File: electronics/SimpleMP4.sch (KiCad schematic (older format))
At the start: 124 parts, among them J1 USB_OTG, J2 DISPLAY, Q1 8050, Q2 SI2305, Q3 SI2305, Q4 8050, Q5 8550, Q6 SI2305, Q7 8550, U1 OCP8020, U2 RK2608, U3 OCP2150TW18A, U4 OCP1240, U5 MT25QL128ABA, U6 K9HCG08U1M-PCB0/PIB0, U7 K4S641632N, U8 TRS_5PIN, U9 MMC/SD_SOCKET, Y1 24MHz

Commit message: added partial routing
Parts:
- L3, L5: footprint (none) -> Inductors_SMD:L_1210
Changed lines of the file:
@@
 F 0 "L5" V 8400 8000 50  0000 C CNN
 F 1 "10uH" V 8525 8000 50  0000 C CNN
-F 2 "" H 8450 8000 50  0001 C CNN
+F 2 "Inductors_SMD:L_1210" H 8450 8000 50  0001 C CNN
 F 3 "" H 8450 8000 50  0001 C CNN
 	1    8450 8000
@@
 F 0 "L3" V 7650 7500 50  0000 C CNN
 F 1 "10uH" V 7775 7500 50  0000 C CNN
-F 2 "" H 7700 7500 50  0001 C CNN
+F 2 "Inductors_SMD:L_1210" H 7700 7500 50  0001 C CNN
 F 3 "" H 7700 7500 50  0001 C CNN
 	1    7700 7500

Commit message: added test points
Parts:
- removed RN1: 5R, Resistors_THT:R_Array_SIP5, symbol R_Network04
- removed RN2: 33R*4, symbol R_Pack04
- added R37, R38, R39, R40: 33R, Resistors_SMD:R_0603, symbol R
- added R41, R42, R43, R44: R*, Resistors_SMD:R_0603, symbol R
- added TP? (x9): TEST, symbol TEST
- B1, B2, B3, B4, B5, B6: footprint SKHLAAA010:SKHLAAA010 -> HP0315AFKP4-R:SW_HP0315AFKP4-R
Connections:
- net BATT: now also TP?.1
- net FALE/RS/A1: now also R38.2
- net GND: now also TP?.1
- net I2C_SCL: now also TP?.1
- net I2C_SDA: now also TP?.1
- net LCDCSN: now also R37.2
- net LCDRDN: now also R40.2
- net LCDWRN: now also R39.2
- net PWR_ON: now also TP?.1
- net SDCLK: now also TP?.1
- net SDDI: now also TP?.1
- net SDDO: now also TP?.1
- net VCC: now also TP?.1
- net at J2.10 (P10): now also R40.1
- net at J2.17 (P17): now also R41.1
- net at J2.18 (P18): now also R42.1
- net at J2.19 (P19): now also R43.1
- net at J2.20 (P20): now also R44.1
- net at J2.7 (P7): now also R37.1
- net at J2.8 (P8): now also R38.1
- net at J2.9 (P9): now also R39.1
- net at C43.2: now also R41.2, R42.2, R43.2, R44.2
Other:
- moved on the sheet: C43, C44, C46, C47, J2, Q7, R35, R36

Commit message: added another data bus
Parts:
- TP1: renamed from TP?; value TEST -> VCC; footprint (none) -> Connectors:PINTST
- TP2: renamed from TP?; value TEST -> GND; footprint (none) -> Connectors:PINTST
- TP3: renamed from TP?; value TEST -> SDDI; footprint (none) -> Connectors:PINTST
- TP4: renamed from TP?; value TEST -> SDDO; footprint (none) -> Connectors:PINTST
- TP5: renamed from TP?; value TEST -> SDCLK; footprint (none) -> Connectors:PINTST
- TP6: renamed from TP?; value TEST -> SDA; footprint (none) -> Connectors:PINTST
- TP7: renamed from TP?; value TEST -> SCL; footprint (none) -> Connectors:PINTST
- TP8: renamed from TP?; value TEST -> BATT; footprint (none) -> Connectors:PINTST
- TP9: renamed from TP?; value TEST -> PWR_ON; footprint (none) -> Connectors:PINTST
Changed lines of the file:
@@
 Connection ~ 13700 3050
 $Comp
-L TEST TP?
+L TEST TP1
 U 1 1 5A44E92B
 P 15450 1200
-F 0 "TP?" H 15450 1500 50  0000 C BNN
-F 1 "TEST" H 15450 1450 50  0000 C CNN
-F 2 "" H 15450 1200 50  0001 C CNN
+F 0 "TP1" H 15450 1500 50  0000 C BNN
+F 1 "VCC" H 15450 1450 50  0000 C CNN
+F 2 "Connectors:PINTST" H 15450 1200 50  0001 C CNN
 F 3 "" H 15450 1200 50  0001 C CNN
 	1    15450 1200
@@
 VCC
 $Comp
-L TEST TP?
+L TEST TP2
 U 1 1 5A44FF22
 P 15450 1400
-F 0 "TP?" H 15450 1700 50  0000 C BNN
-F 1 "TEST" H 15450 1650 50  0000 C CNN
-F 2 "" H 15450 1400 50  0001 C CNN
+F 0 "TP2" H 15450 1700 50  0000 C BNN
+F 1 "GND" H 15450 1650 50  0000 C CNN
+F 2 "Connectors:PINTST" H 15450 1400 50  0001 C CNN
 F 3 "" H 15450 1400 50  0001 C CNN
 	1    15450 1400
@@
 GND
 $Comp
-L TEST TP?
+L TEST TP3
 U 1 1 5A450D61
 P 15450 1600
-F 0 "TP?" H 15450 1900 50  0000 C BNN
-F 1 "TEST" H 15450 1850 50  0000 C CNN
-F 2 "" H 15450 1600 50  0001 C CNN
+F 0 "TP3" H 15450 1900 50  0000 C BNN
+F 1 "SDDI" H 15450 1850 50  0000 C CNN
+F 2 "Connectors:PINTST" H 15450 1600 50  0001 C CNN
 F 3 "" H 15450 1600 50  0001 C CNN
 	1    15450 1600
@@
 	15250 1600 15450 1600
 $Comp
-L TEST TP?
+L TEST TP4
 U 1 1 5A452A41
 P 15450 1800
-F 0 "TP?" H 15450 2100 50  0000 C BNN
-F 1 "TEST" H 15450 2050 50  0000 C CNN
-F 2 "" H 15450 1800 50  0001 C CNN
+F 0 "TP4" H 15450 2100 50  0000 C BNN
+F 1 "SDDO" H 15450 2050 50  0000 C CNN
+F 2 "Connectors:PINTST" H 15450 1800 50  0001 C CNN
 F 3 "" H 15450 1800 50  0001 C CNN
 	1    15450 1800
@@
 	15450 1800 15250 1800
 $Comp
-L TEST TP?
+L TEST TP5
 U 1 1 5A4542A1
 P 15450 2000
-F 0 "TP?" H 15450 2300 50  0000 C BNN
-F 1 "TEST" H 15450 2250 50  0000 C CNN
-F 2 "" H 15450 2000 50  0001 C CNN
+F 0 "TP5" H 15450 2300 50  0000 C BNN
+F 1 "SDCLK" H 15450 2250 50  0000 C CNN
+F 2 "Connectors:PINTST" H 15450 2000 50  0001 C CNN
 F 3 "" H 15450 2000 50  0001 C CNN
 	1    15450 2000
@@
 SDCLK
 $Comp
-L TEST TP?
+L TEST TP6
 U 1 1 5A455DCF
 P 15450 2200
-F 0 "TP?" H 15450 2500 50  0000 C BNN
-F 1 "TEST" H 15450 2450 50  0000 C CNN
-F 2 "" H 15450 2200 50  0001 C CNN
+F 0 "TP6" H 15450 2500 50  0000 C BNN
+F 1 "SDA" H 15450 2450 50  0000 C CNN
+F 2 "Connectors:PINTST" H 15450 2200 50  0001 C CNN
 F 3 "" H 15450 2200 50  0001 C CNN
 	1    15450 2200
@@
 	15450 2200 15200 2200
 $Comp
-L TEST TP?
+L TEST TP7
 U 1 1 5A4572CC
 P 15450 2400
-F 0 "TP?" H 15450 2700 50  0000 C BNN
-F 1 "TEST" H 15450 2650 50  0000 C CNN
-F 2 "" H 15450 2400 50  0001 C CNN
+F 0 "TP7" H 15450 2700 50  0000 C BNN
+F 1 "SCL" H 15450 2650 50  0000 C CNN
+F 2 "Connectors:PINTST" H 15450 2400 50  0001 C CNN
 F 3 "" H 15450 2400 50  0001 C CNN
 	1    15450 2400
@@
 I2C_SCL
 $Comp
-L TEST TP?
+L TEST TP8
 U 1 1 5A458D47
 P 15450 2600
-F 0 "TP?" H 15450 2900 50  0000 C BNN
-F 1 "TEST" H 15450 2850 50  0000 C CNN
-F 2 "" H 15450 2600 50  0001 C CNN
+F 0 "TP8" H 15450 2900 50  0000 C BNN
+F 1 "BATT" H 15450 2850 50  0000 C CNN
+F 2 "Connectors:PINTST" H 15450 2600 50  0001 C CNN
 F 3 "" H 15450 2600 50  0001 C CNN
 	1    15450 2600
@@
 PWR_ON
 $Comp
-L TEST TP?
+L TEST TP9
 U 1 1 5A45AAA3
 P 15450 2800
-F 0 "TP?" H 15450 3100 50  0000 C BNN
-F 1 "TEST" H 15450 3050 50  0000 C CNN
-F 2 "" H 15450 2800 50  0001 C CNN
+F 0 "TP9" H 15450 3100 50  0000 C BNN
+F 1 "PWR_ON" H 15450 3050 50  0000 C CNN
+F 2 "Connectors:PINTST" H 15450 2800 50  0001 C CNN
 F 3 "" H 15450 2800 50  0001 C CNN
 	1    15450 2800

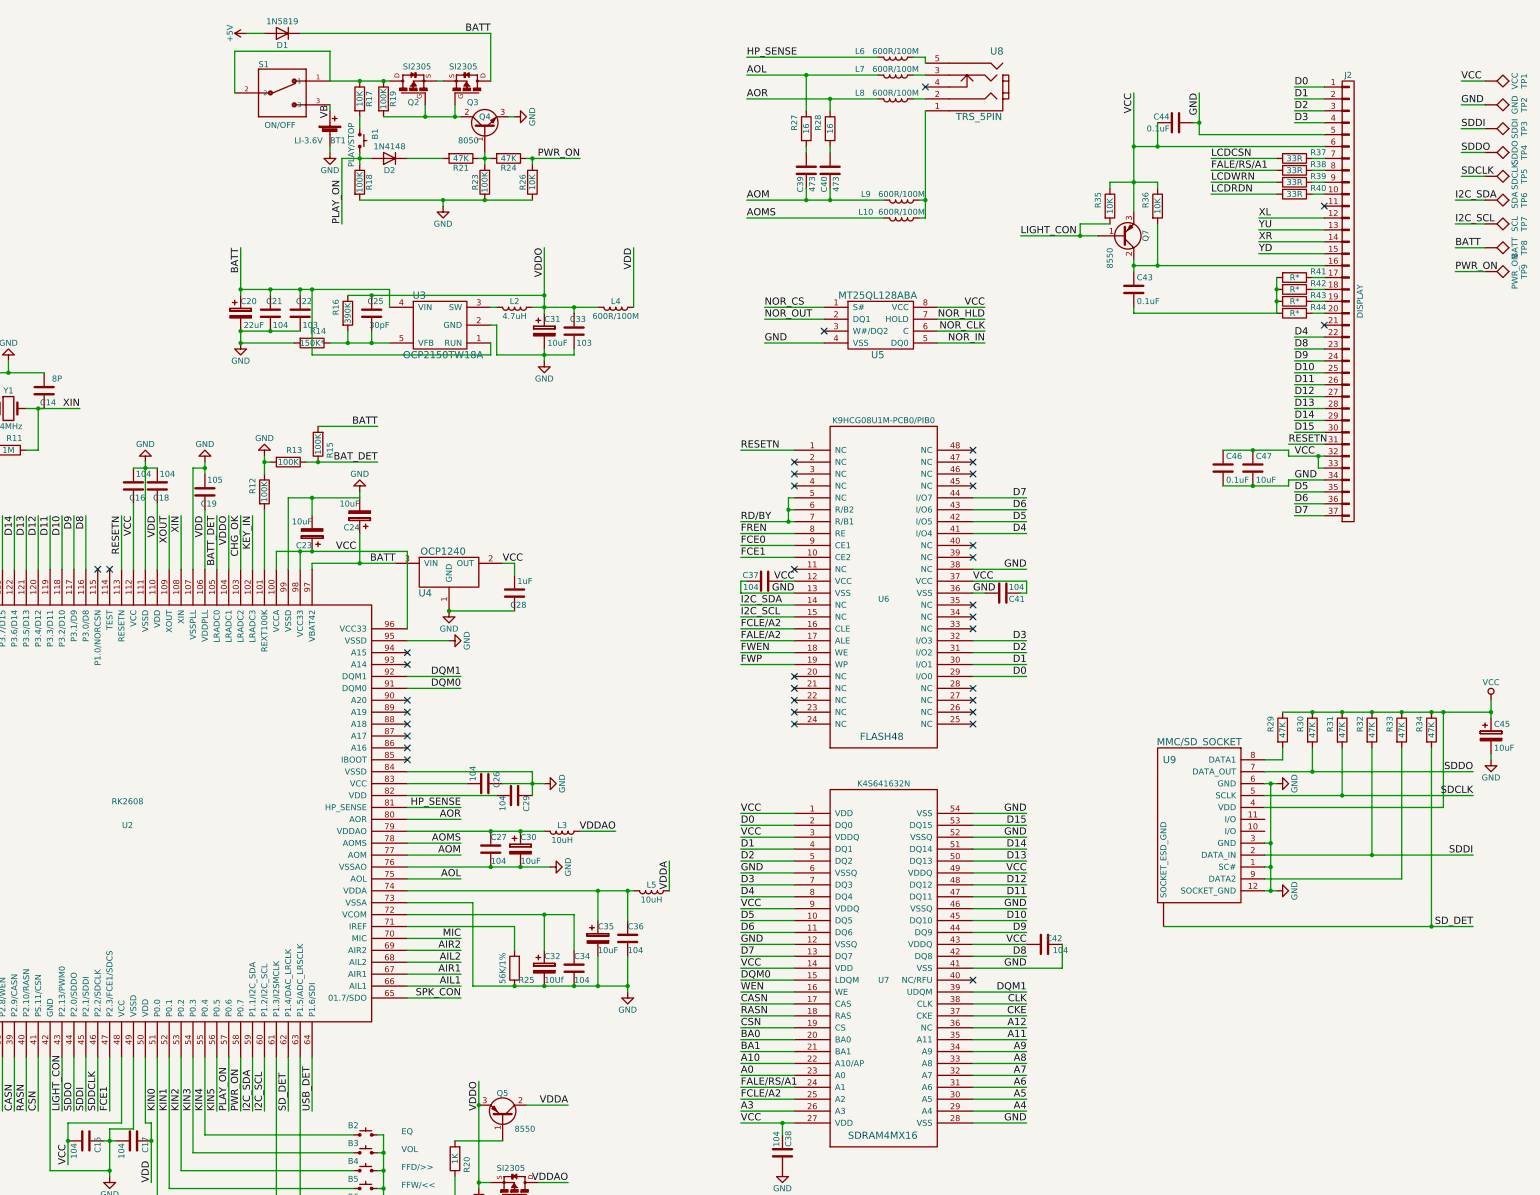
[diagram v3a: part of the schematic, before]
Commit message: added routing to buttons
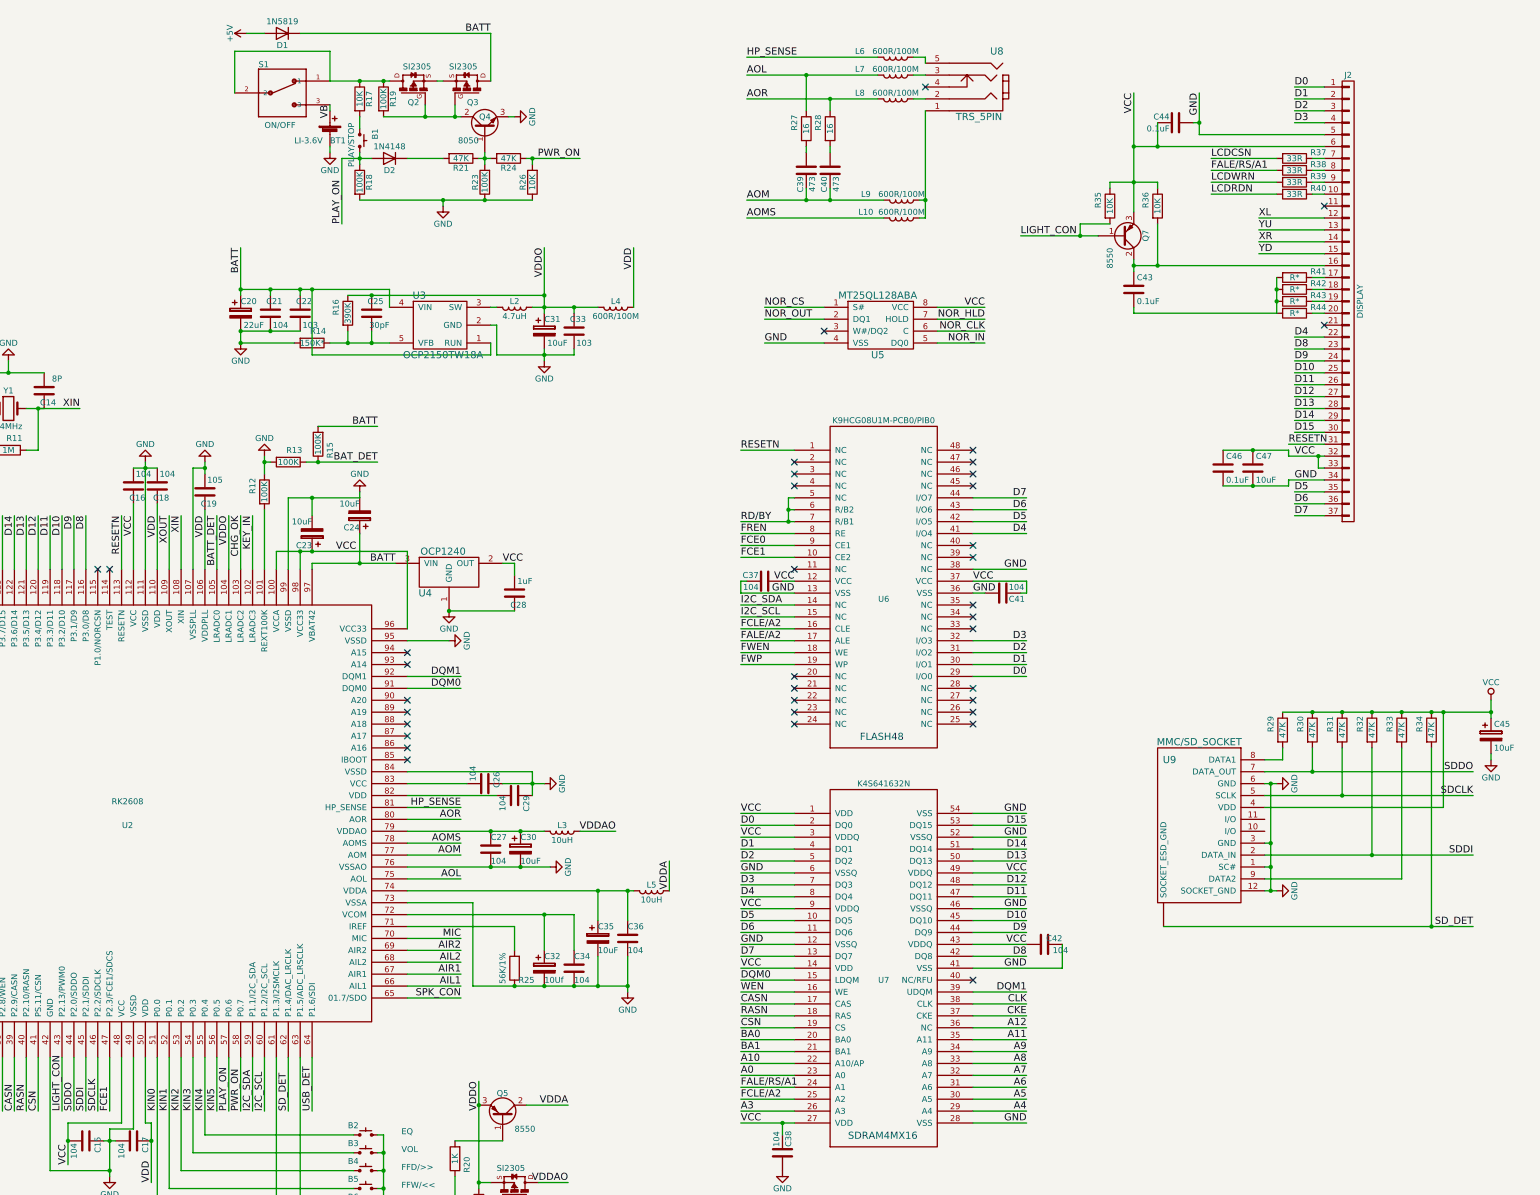
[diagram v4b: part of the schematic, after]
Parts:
- removed TP1: VCC, Connectors:PINTST, symbol TEST
- removed TP2: GND, Connectors:PINTST, symbol TEST
- removed TP3: SDDI, Connectors:PINTST, symbol TEST
- removed TP4: SDDO, Connectors:PINTST, symbol TEST
- removed TP5: SDCLK, Connectors:PINTST, symbol TEST
- removed TP6: SDA, Connectors:PINTST, symbol TEST
- removed TP7: SCL, Connectors:PINTST, symbol TEST
- removed TP8: BATT, Connectors:PINTST, symbol TEST
- removed TP9: PWR_ON, Connectors:PINTST, symbol TEST
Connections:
- net SDDCLK is gone; now on net SDCLK: U2.46 (P2.2/SDCLK)
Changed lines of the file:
@@
 SDDI
 Text Label 3800 9850 1    60   ~ 0
-SDDCLK
+SDCLK
 Text Label 3900 9850 1    60   ~ 0
 FCE1
@@
 Connection ~ 13700 2950
 Connection ~ 13700 3050
-$Comp
-L TEST TP1
-U 1 1 5A44E92B
-P 15450 1200
-F 0 "TP1" H 15450 1500 50  0000 C BNN
-F 1 "VCC" H 15450 1450 50  0000 C CNN
-F 2 "Connectors:PINTST" H 15450 1200 50  0001 C CNN
-F 3 "" H 15450 1200 50  0001 C CNN
-	1    15450 1200
-	0    1    1    0
-$EndComp
-Wire Wire Line
-	15450 1200 15250 1200
-Text Label 15250 1200 0    60   ~ 0
-VCC
-$Comp
-L TEST TP2
-U 1 1 5A44FF22
-P 15450 1400
-F 0 "TP2" H 15450 1700 50  0000 C BNN
-F 1 "GND" H 15450 1650 50  0000 C CNN
-F 2 "Connectors:PINTST" H 15450 1400 50  0001 C CNN
-F 3 "" H 15450 1400 50  0001 C CNN
-	1    15450 1400
-	0    1    1    0
-$EndComp
-Wire Wire Line
-	15450 1400 15250 1400
-Text Label 15250 1400 0    60   ~ 0
-GND
-$Comp
-L TEST TP3
-U 1 1 5A450D61
-P 15450 1600
-F 0 "TP3" H 15450 1900 50  0000 C BNN
-F 1 "SDDI" H 15450 1850 50  0000 C CNN
-F 2 "Connectors:PINTST" H 15450 1600 50  0001 C CNN
-F 3 "" H 15450 1600 50  0001 C CNN
-	1    15450 1600
-	0    1    1    0
-$EndComp
-Text Label 15250 1600 0    60   ~ 0
-SDDI
-Wire Wire Line
-	15250 1600 15450 1600
-$Comp
-L TEST TP4
-U 1 1 5A452A41
-P 15450 1800
-F 0 "TP4" H 15450 2100 50  0000 C BNN
-F 1 "SDDO" H 15450 2050 50  0000 C CNN
-F 2 "Connectors:PINTST" H 15450 1800 50  0001 C CNN
-F 3 "" H 15450 1800 50  0001 C CNN
-	1    15450 1800
-	0    1    1    0
-$EndComp
-Text Label 15250 1800 0    60   ~ 0
-SDDO
-Wire Wire Line
-	15450 1800 15250 1800
-$Comp
-L TEST TP5
-U 1 1 5A4542A1
-P 15450 2000
-F 0 "TP5" H 15450 2300 50  0000 C BNN
-F 1 "SDCLK" H 15450 2250 50  0000 C CNN
-F 2 "Connectors:PINTST" H 15450 2000 50  0001 C CNN
-F 3 "" H 15450 2000 50  0001 C CNN
-	1    15450 2000
-	0    1    1    0
-$EndComp
-Wire Wire Line
-	15450 2000 15250 2000
-Text Label 15250 2000 0    60   ~ 0
-SDCLK
-$Comp
-L TEST TP6
-U 1 1 5A455DCF
-P 15450 2200
-F 0 "TP6" H 15450 2500 50  0000 C BNN
-F 1 "SDA" H 15450 2450 50  0000 C CNN
-F 2 "Connectors:PINTST" H 15450 2200 50  0001 C CNN
-F 3 "" H 15450 2200 50  0001 C CNN
-	1    15450 2200
-	0    1    1    0
-$EndComp
-Text Label 15200 2200 0    60   ~ 0
-I2C_SDA
-Wire Wire Line
-	15450 2200 15200 2200
-$Comp
-L TEST TP7
-U 1 1 5A4572CC
-P 15450 2400
-F 0 "TP7" H 15450 2700 50  0000 C BNN
-F 1 "SCL" H 15450 2650 50  0000 C CNN
-F 2 "Connectors:PINTST" H 15450 2400 50  0001 C CNN
-F 3 "" H 15450 2400 50  0001 C CNN
-	1    15450 2400
-	0    1    1    0
-$EndComp
-Wire Wire Line
-	15450 2400 15200 2400
-Text Label 15200 2400 0    60   ~ 0
-I2C_SCL
-$Comp
-L TEST TP8
-U 1 1 5A458D47
-P 15450 2600
-F 0 "TP8" H 15450 2900 50  0000 C BNN
-F 1 "BATT" H 15450 2850 50  0000 C CNN
-F 2 "Connectors:PINTST" H 15450 2600 50  0001 C CNN
-F 3 "" H 15450 2600 50  0001 C CNN
-	1    15450 2600
-	0    1    1    0
-$EndComp
-Wire Wire Line
-	15450 2600 15200 2600
-Text Label 15200 2600 0    60   ~ 0
-BATT
-Text Label 15200 2800 0    60   ~ 0
-PWR_ON
-$Comp
-L TEST TP9
-U 1 1 5A45AAA3
-P 15450 2800
-F 0 "TP9" H 15450 3100 50  0000 C BNN
-F 1 "PWR_ON" H 15450 3050 50  0000 C CNN
-F 2 "Connectors:PINTST" H 15450 2800 50  0001 C CNN
-F 3 "" H 15450 2800 50  0001 C CNN
-	1    15450 2800
-	0    1    1    0
-$EndComp
-Wire Wire Line
-	15200 2800 15450 2800
 $EndSCHEMATC

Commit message: 94 unconnected left
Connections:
- net I2C_SCL: no longer U6.15 (NC)
- net I2C_SDA: no longer U6.14 (NC)
- no-connect marks 37 -> 39
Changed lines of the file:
@@
 Text Label 9200 5200 0    60   ~ 0
 FCE1
-Text Label 9200 5600 0    60   ~ 0
-I2C_SDA
-Text Label 9200 5700 0    60   ~ 0
-I2C_SCL
 Text Label 9200 5800 0    60   ~ 0
 FCLE/A2
@@
 	9200 5500 9650 5500
 Wire Wire Line
-	9650 5600 9200 5600
-Wire Wire Line
-	9650 5700 9200 5700
-Wire Wire Line
 	9650 5800 9200 5800
 Wire Wire Line
@@
 Connection ~ 12500 2750
 Wire Wire Line
-	12500 3150 13700 3150
+	13700 3150 12500 3150
 Wire Wire Line
 	12500 3150 12500 3100
@@
 $EndComp
 Wire Wire Line
-	13700 3150 13700 2850
+	13700 2850 13700 3150
 Connection ~ 13700 2950
 Connection ~ 13700 3050
+NoConn ~ 9650 5600
+NoConn ~ 9650 5700
 $EndSCHEMATC

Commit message: added OSHpark renders
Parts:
- B1, B2, B3, B4, B5, B6: footprint HP0315AFKP4-R:SW_HP0315AFKP4-R -> footprints:SW_HP0315AFKP4-R
- BT1: footprint Connectors_JST:JST_PH_B2B-PH-SM4-TB_02x2.00mm_Straight -> footprints:JST_PH_B2B-PH-SM4-TB_02x2.00mm_Straight
- C1, C10, C11, C12, C13, C14, C15, C16, C17, C18, C19, C2, C21, C22, C25, C26, C27, C28, C29, C3, C33, C34, C36, C37, C38, C39, C4, C40, C41, C42, C43, C44, C46, C47, C7, C8, C9: footprint Capacitors_SMD:C_0603 -> footprints:C_0603
- C20, C23, C24, C30, C31, C32, C35, C45, C5, C6: footprint Capacitors_SMD:CP_Elec_4x4.5 -> footprints:CP_Elec_4x4.5
- D1, D2: footprint Diodes_SMD:D_SOD-123 -> footprints:D_SOD-123
- J1: footprint Connectors:USB_Mini-B -> footprints:USB_Mini-B
- L1, L10, L4, L6, L7, L8, L9: footprint Inductors_SMD:L_0603 -> footprints:L_0603
- L3, L5: footprint Inductors_SMD:L_1210 -> footprints:L_1210
- Q1, Q2, Q3, Q4, Q5, Q6, Q7, U4: footprint TO_SOT_Packages_SMD:SOT-23 -> footprints:SOT-23
- R1, R10, R11, R12, R13, R14, R15, R16, R17, R18, R19, R2, R20, R21, R22, R23, R24, R25, R26, R27, R28, R29, R3, R30, R31, R32, R33, R34, R35, R36, R37, R38, R39, R4, R40, R41, R42, R43, R44, R5, R6, R7, R8, R9: footprint Resistors_SMD:R_0603 -> footprints:R_0603
- S1: footprint SS312SAH4-R:SW_SS312SAH4-R -> footprints:SW_SS312SAH4-R
- U1, U3: footprint TO_SOT_Packages_SMD:SOT-23-5 -> footprints:SOT-23-5
- U2: footprint Housings_QFP:LQFP-128_14x14mm_Pitch0.4mm -> footprints:LQFP-128_14x14mm_Pitch0.4mm
- U6: footprint Housings_SSOP:TSOP-I-48_18.4x12mm_Pitch0.5mm -> footprints:TSOP-I-48_18.4x12mm_Pitch0.5mm
- U7: footprint TSOP-54:TSOP-54 -> footprints:TSOP-54
- U8: footprint Connectors:Stereo_Jack_3.5mm_Switch_Ledino_KB3SPRS -> footprints:Stereo_Jack_3.5mm_Switch_Ledino_KB3SPRS
- U9: footprint Connectors:SD_Card_Receptacle -> footprints:SD_Card_Receptacle
- Y1: footprint Crystals:Crystal_SMD_HC49-SD -> footprints:Crystal_SMD_HC49-SD
